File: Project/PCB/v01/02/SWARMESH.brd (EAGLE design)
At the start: 75 x 75 mm, 48 parts, among them IC1 4051N, M1 MOTOR10MM, M2 MOTOR10MM, Q1 TIP122, U1 ESP32DEVKITC, U2 TCRT5000L, U3 L293D, U4 7805T, U5 TCRT5000L

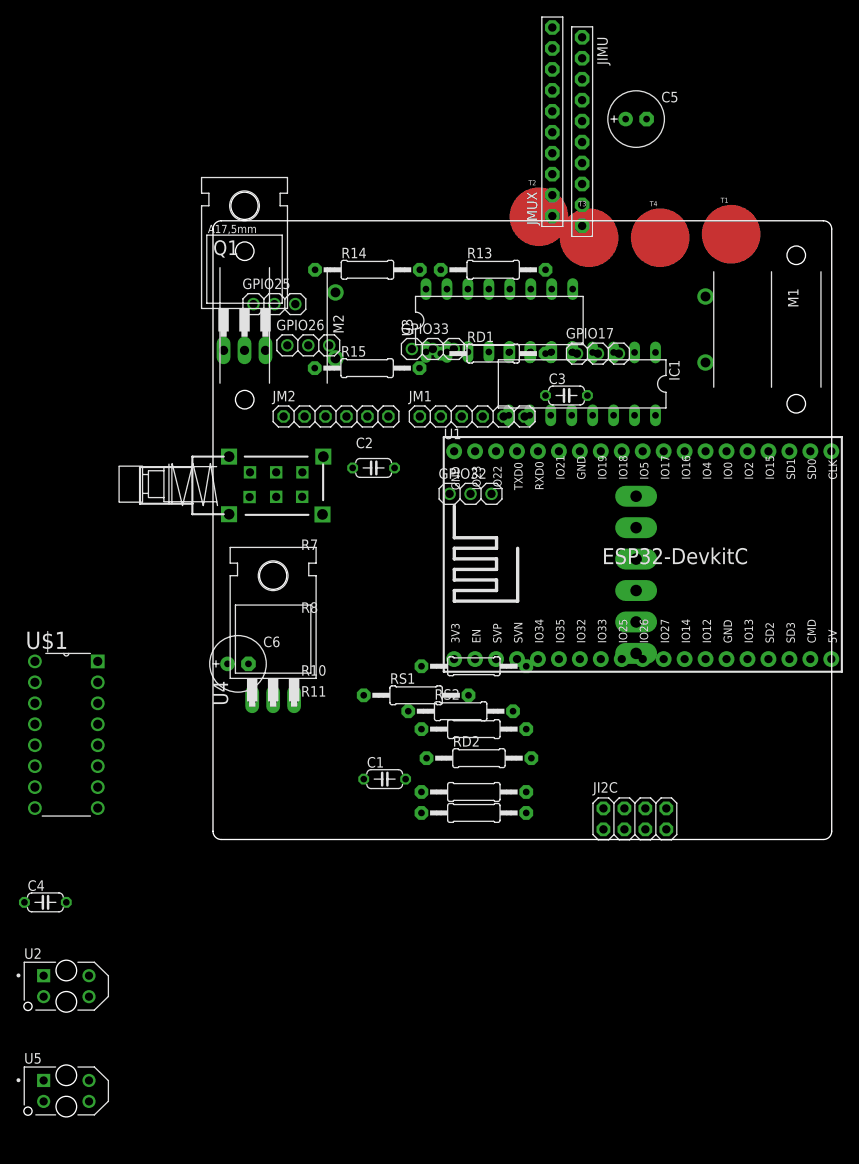
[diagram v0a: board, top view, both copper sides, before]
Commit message: update schematic
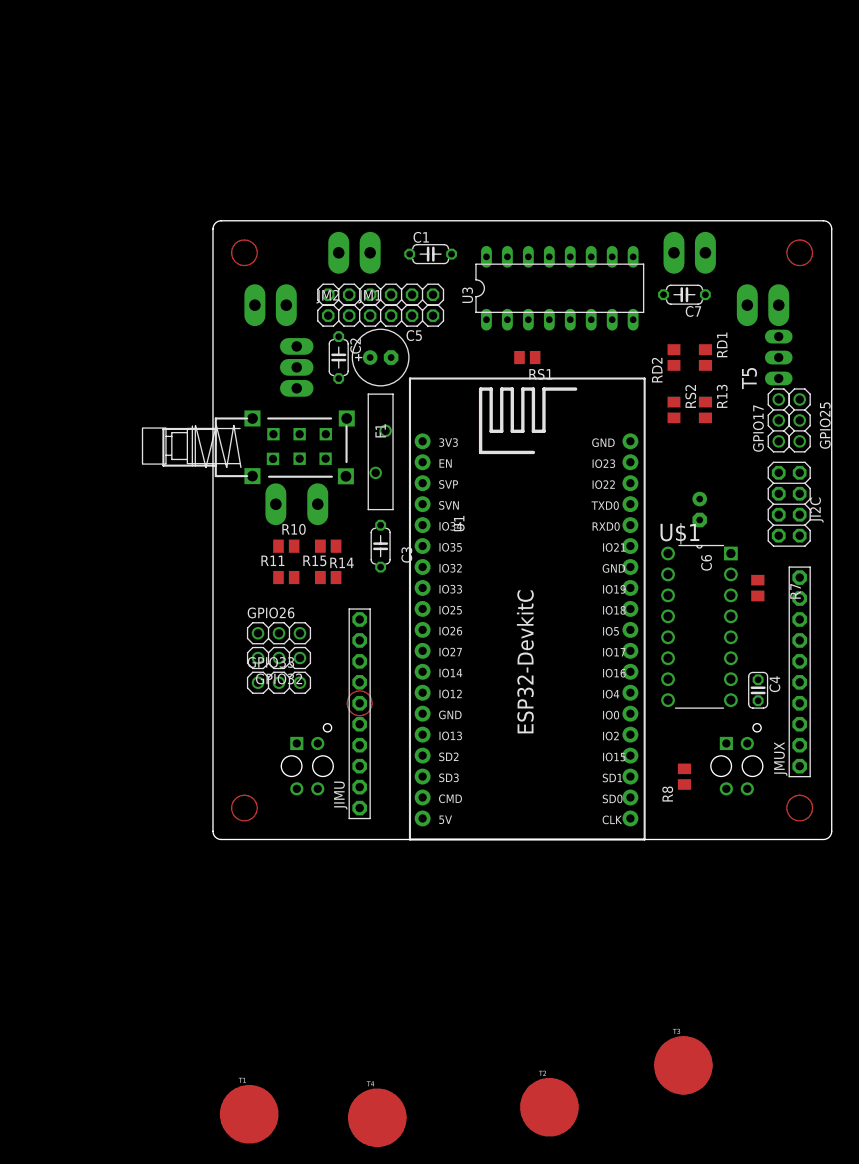
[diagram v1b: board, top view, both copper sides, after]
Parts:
- removed IC1: 4051N, 40xx:DIL16
- removed M1, M2: MOTOR10MM, SparkFun-Electromechanical:VIBE-MOTOR-10MM
- removed Q1: TIP122, transistor-npn:TO220
- added C7: 0.1uF, adafruit:C050-024X044
- added F1: 30R400UF, 30R400UF:30R400UF
- added JP1, JP2, JP3, JP4: (no value), adafruit:1X1-BIGPOGO
- added T5: TIP122TIP122, TIP122(2):TIP122MODIFIED
- C4: device adafruit:C050-024X044 -> rcl:C025-024X044
- R10, R11, R13, R14, R15, R7, R8, RD1, RD2, RS1, RS2: device adafruit:0207/12 -> adafruit:M0805
- U4: value 7805T -> L7805CV; device adafruit:TO220H -> L7805:L7805CV_FOOTPRINT
- moved T1 121.6 mm to (4.39, -33.3)
- moved T4 112.1 mm to (19.9, -33.7)
- moved T2 108.0 mm to (40.8, -32.5)
- moved T3 101.0 mm to (57.0, -27.4)
- moved U5 90.3 mm to (63.5, 8.89), flipped to the bottom, turned to 270 degrees
- moved C4 90.1 mm to (66.1, 18.1), turned to 270 degrees
- moved U$1 77.9 mm to (59.0, 25.8)
- moved JIMU 75.5 mm to (17.8, 15.2), turned to 90 degrees
- moved JMUX 73.1 mm to (71.1, 20.3)
- moved GPIO25 65.2 mm to (71.1, 50.8), turned to 90 degrees
- moved C1 63.9 mm to (26.4, 71.0)
- moved C6 59.0 mm to (59.0, 40.0), flipped to the bottom, turned to 270 degrees
- moved CHG1- 57.2 mm to (8.89, 64.8), turned to 270 degrees
- moved RD2 54.0 mm to (55.9, 58.4), turned to 90 degrees
- moved BAT+ 51.7 mm to (5.08, 64.8), turned to 90 degrees
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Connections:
- removed net N$21: BAT+.P$1, S2.NC1
- removed net N$37: Q1.2, RD1.1
- removed net N$38: R15.2
- new net N$12: R13.1, T5.1
- new net N$15: BAT+.P$1, CHG1+.P$1, CHG2+.P$1, F1.1
- new net N$18: F1.2, S2.NC1
- net GND: now also T5.3; no longer C1.2, IC1.7, IC1.8, Q1.3, U4.2
- net M1A: now also C1.1, JP1.P$1; no longer M1.+
- net M1B: now also C1.2, JP2.P$1; no longer M1.-
- net M2A: now also C7.1, JP4.P$1; no longer M2.-
- net M2B: now also C7.2, JP3.P$1; no longer M2.+
- net N$1: now also RD1.1, T5.2; no longer Q1.1, R13.1
- net V+: now also R15.2; no longer CHG1+.P$1, CHG2+.P$1
- net VCC: no longer C1.1, IC1.16

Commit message: minor update
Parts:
- removed U$1: CD4051BEE4, CD4051BEE4:CD4051BEE4DIP
- added U6: CD4051BEE4, CD4051BEE4:CD4051BEE4DIP
- moved C6 5.24 mm to (57.7, 45.1), turned to 0 degrees
- moved JMUX 1.27 mm to (71.1, 21.6)
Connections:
- removed net N$2: JMUX.1, U$1.13
- removed net N$3: JMUX.2, U$1.14
- removed net N$4: JMUX.3, U$1.15
- removed net N$6: JMUX.4, U$1.12
- new net ADCMX1: U6.3
- new net N$19: JMUX.1, U6.13
- new net N$20: JMUX.2, U6.14
- new net N$21: JMUX.4, U6.12
- new net N$22: JMUX.3, U6.15
- net ADCMX: no longer U$1.3
- net GND: no longer U$1.6, U$1.7, U$1.8
- net IO5: now also U6.11; no longer U$1.11
- net N$11: now also U6.1; no longer U$1.1
- net N$12: now also U6.6, U6.7, U6.8
- net N$13: now also U6.2; no longer U$1.2
- net N$14: now also U6.5; no longer U$1.5
- net N$5: now also U6.4; no longer U$1.4
- net N$7: now also U6.10; no longer U$1.10
- net N$8: now also U6.9; no longer U$1.9
- net VCC: now also U6.16; no longer U$1.16
